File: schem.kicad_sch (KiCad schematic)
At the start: 7 parts, among them U1 TP4056 module

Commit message: Update Schematic
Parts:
- added SW1: SW_SPST, symbol Switch:SW_SPST
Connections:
- net at U1.6 (OUT+): now also SW1.2 (B); no longer A1.39 (VSYS)
- new net: A1.39 (VSYS), SW1.1 (A)
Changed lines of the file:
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@@
 	(wire
 		(pts
-			(xy 118.11 16.51) (xy 53.34 16.51)
+			(xy 118.11 16.51) (xy 100.33 16.51)
+		)
+		(stroke
+			(width 0)
+			(type default)
+		)
+	)
+	(wire
+		(pts
+			(xy 90.17 16.51) (xy 53.34 16.51)
 		)
 		(stroke
@@
 					(unit 1)
 				)
+			)
+		)
+	)
+	(symbol
+		(lib_id "Switch:SW_SPST")
+		(at 95.25 16.51 0)
+		(unit 1)
+		(body_style 1)
+		(exclude_from_sim no)
+		(in_bom yes)
+		(on_board yes)
+		(in_pos_files yes)
+		(dnp no)
+		(property "Reference" "SW1"
+			(at 95.25 18.542 0)
+			(show_name no)
+			(do_not_autoplace no)
+			(effects
+				(font
+					(size 1.27 1.27)
+				)
+			)
+		)
+		(property "Value" "SW_SPST"
+			(at 95.25 21.082 0)
+			(show_name no)
+			(do_not_autoplace no)
+			(effects
+				(font
+					(size 1.27 1.27)
+				)
+			)
+		)
+		(property "Footprint" ""
+			(at 95.25 16.51 0)
+			(hide yes)
+			(show_name no)
+			(do_not_autoplace no)
+			(effects
+				(font
+					(size 1.27 1.27)
+				)
+			)
+		)
+		(property "Datasheet" ""
+			(at 95.25 16.51 0)
+			(hide yes)
+			(show_name no)
+			(do_not_autoplace no)
+			(effects
+				(font
+					(size 1.27 1.27)
+				)
+			)
+		)
+		(property "Description" "Single Pole Single Throw (SPST) switch"
+			(at 95.25 16.51 0)
+			(hide yes)
+			(show_name no)
+			(do_not_autoplace no)
+			(effects
+				(font
+					(size 1.27 1.27)
+				)
+			)
+		)
+		(pin "1"
+		)
+		(pin "2"
+		)
+		(instances
+			(project "schem"
+				(path "/2446c2a2-99a1-4fb5-976e-2f0b9073cc8d"
+					(reference "SW1")
+					(unit 1)
+				)

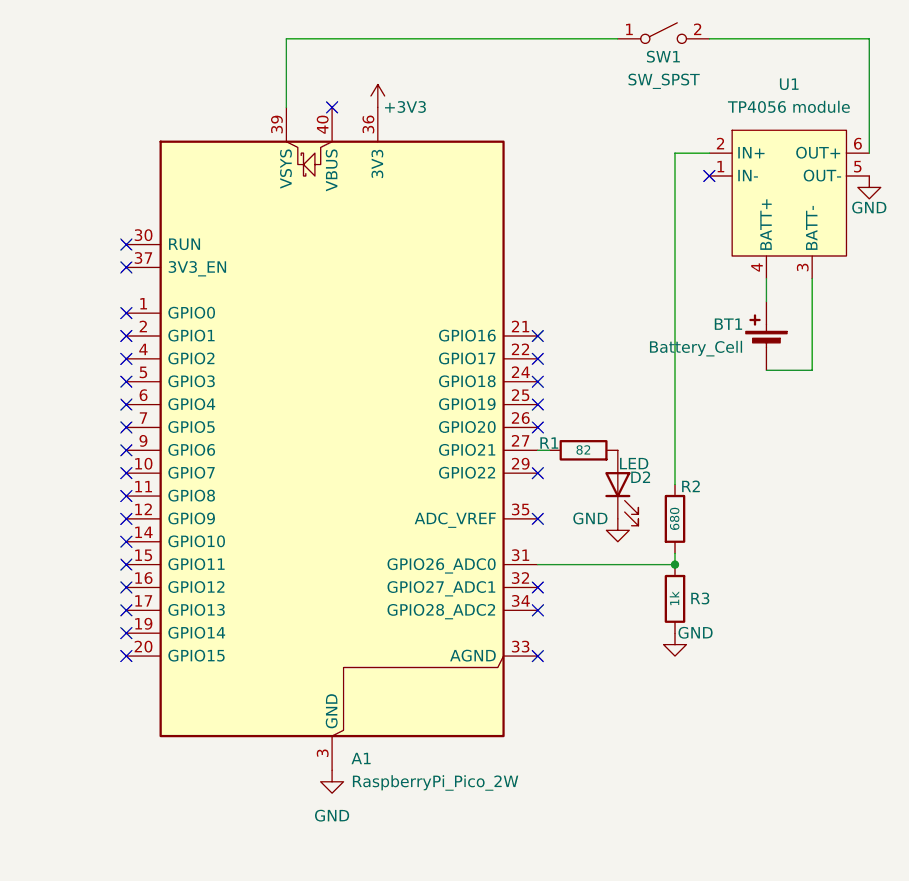
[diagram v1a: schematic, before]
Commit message: Add labels to the schematic
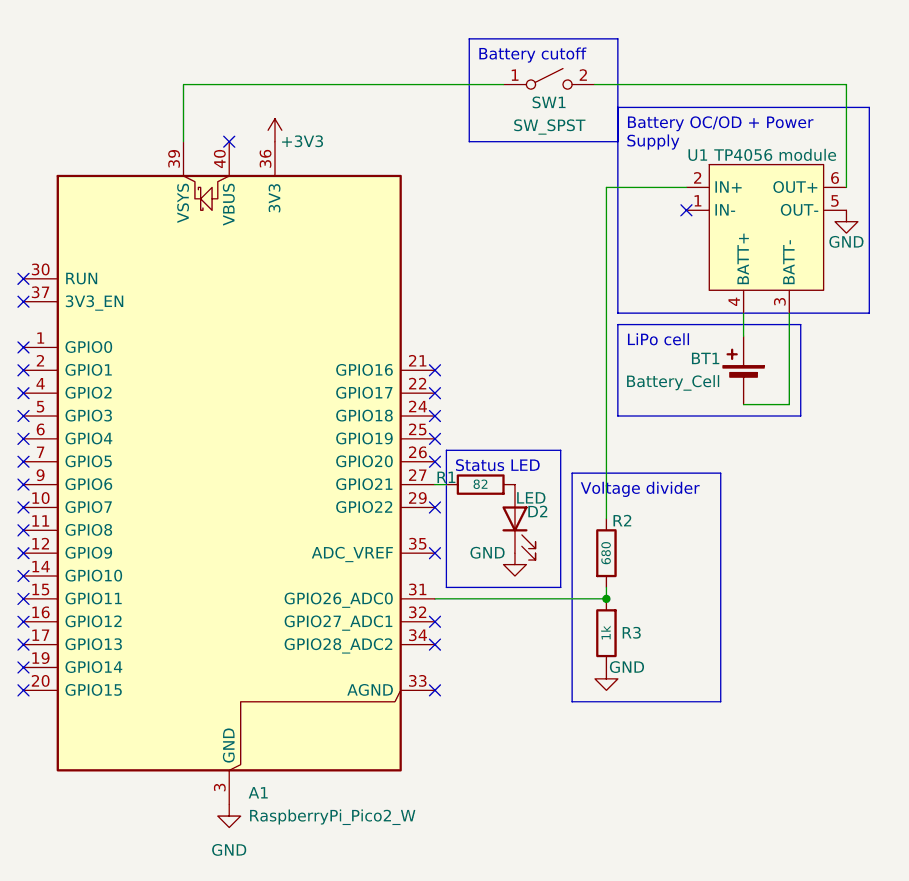
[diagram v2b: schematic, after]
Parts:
- A1: value RaspberryPi_Pico_2W -> RaspberryPi_Pico2_W
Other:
- moved on the sheet: A1, BT1, D2, R1, R2, R3, SW1, U1
